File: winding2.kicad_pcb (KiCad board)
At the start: 2 copper layers, 104 x 75.2 mm, 19 parts, among them J1 Screw_Terminal_2_P5.00mm, J2 Limit Switches, J3 Screw Stepper, J4 Main Stepper, J5 RPM & ESC, J6 5V input, J7 ESC XT60, J8 ARDUINO PROG., SW1 RotaryEncoder_Switch, U1 TMC2209_SILENTSTEPSTICK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

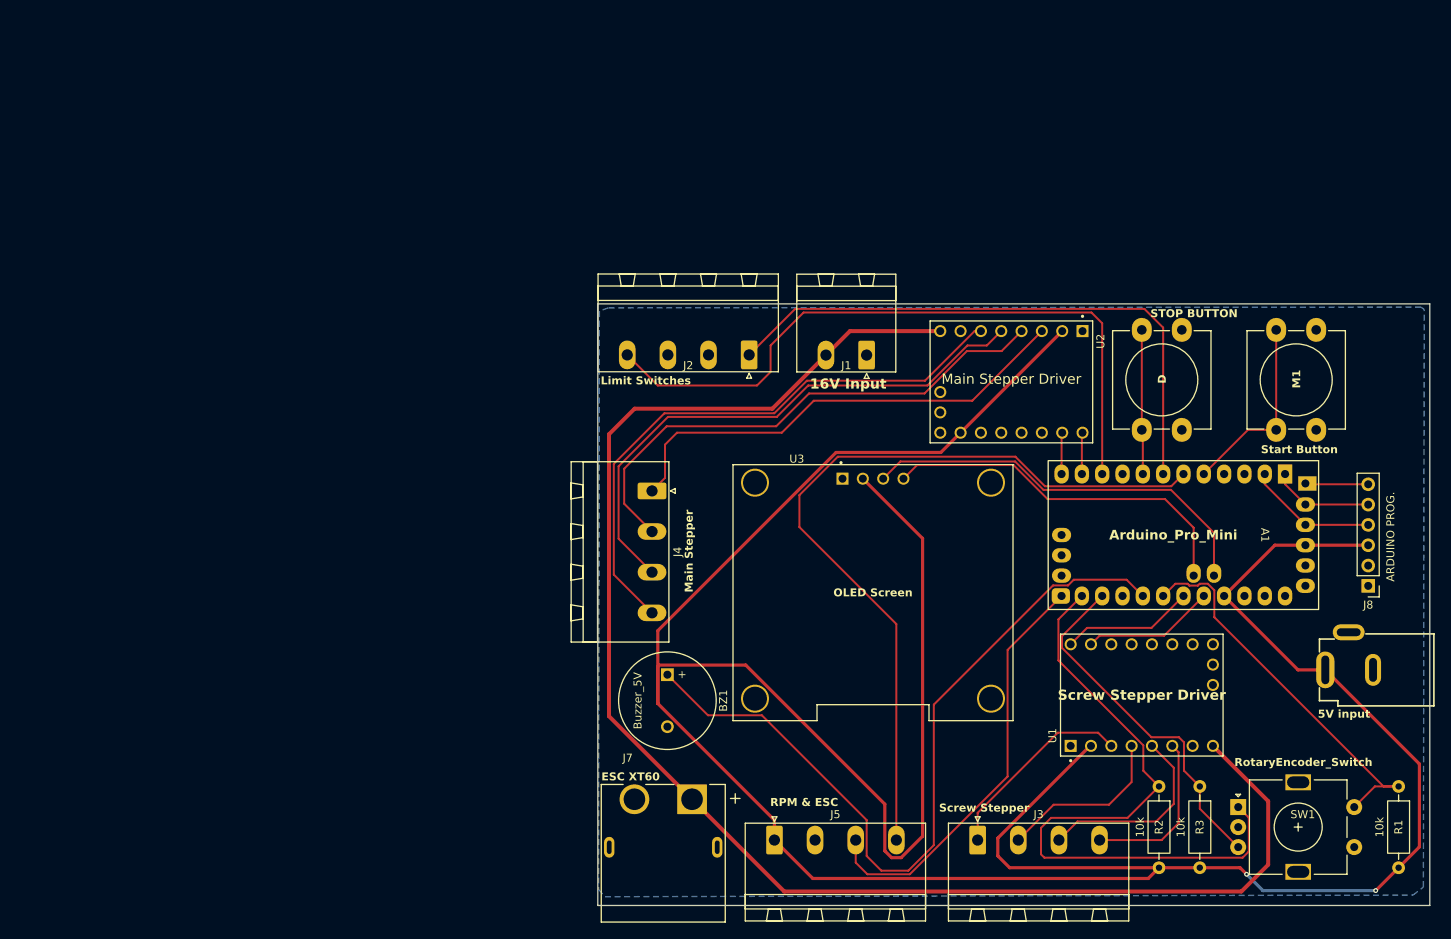
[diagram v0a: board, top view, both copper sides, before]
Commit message: rearranging components to be more user freindly and added front GND Zone
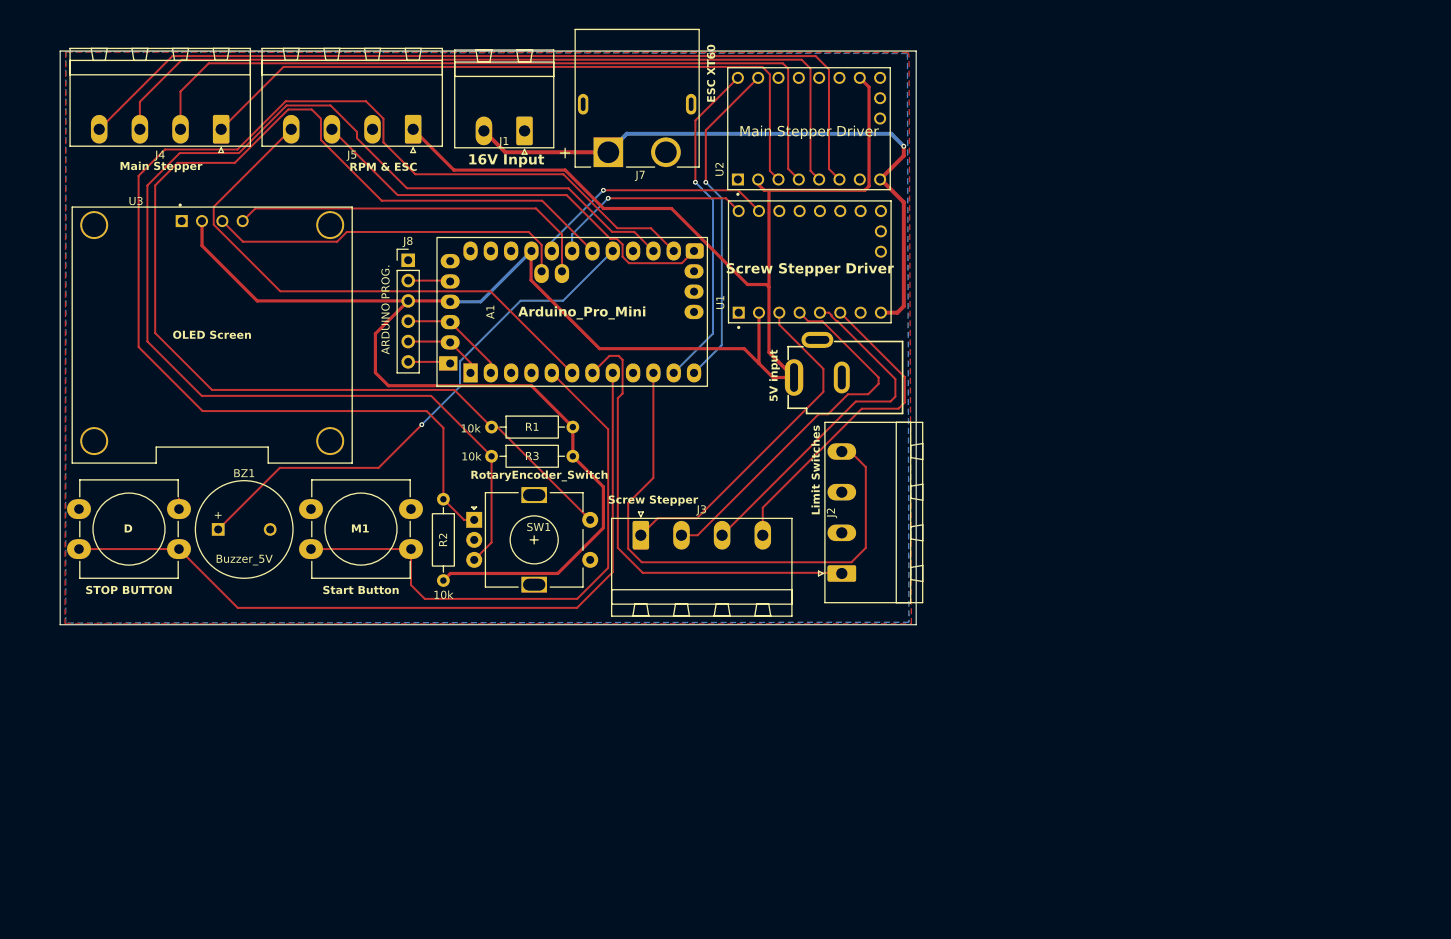
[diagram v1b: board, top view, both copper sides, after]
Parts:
- moved STOP BUTTON 130.4 mm to (56.6, 102.5), turned to 180 degrees
- moved J8 126.7 mm to (91.5, 69.0), turned to 0 degrees
- moved R1 122.0 mm to (101.9, 89.8), turned to 0 degrees
- moved Start Button 118.4 mm to (85.6, 102.5), turned to 180 degrees
- moved A1 102.6 mm to (99.3, 83.0), turned to 90 degrees
- moved SW1 102.0 mm to (99.8, 101.4)
- moved J5 99.7 mm to (92.1, 52.6), turned to 180 degrees
- moved R3 97.7 mm to (101.9, 93.5), turned to 0 degrees
- moved R2 96.4 mm to (95.9, 98.8)
- moved U3 88.7 mm to (67.0, 78.3)
- moved J7 80.9 mm to (120.1, 55.4), turned to 180 degrees
- moved J6 75.8 mm to (145.7, 83.6)
- moved J4 70.3 mm to (68.1, 52.6), turned to 180 degrees
- moved U1 68.2 mm to (141.7, 69.1)
- moved BZ1 59.0 mm to (67.8, 102.6), turned to 0 degrees
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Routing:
- net /ENCODER_B: track 44.6 -> 157.7 mm
- net +16V: track 192.6 -> 81.2 mm, vias 0 -> 1
- net 5V: track 388.5 -> 283.4 mm, vias 2 -> 0
- net /ENCODER_SW: track 49.3 -> 150.0 mm
- net /D_Button: track 18.1 -> 96.5 mm
- net /ENCODER_A: track 83.0 -> 157.8 mm
- net /M1_Button: track 23.8 -> 71.3 mm
- net /DIR1: track 5.20 -> 42.0 mm, vias 0 -> 1
- net /STP1: track 5.20 -> 41.9 mm, vias 0 -> 1
- net /M2B: track 73.4 -> 110.0 mm
- net /M2A: track 69.8 -> 104.2 mm
- net /BUZZ-A0: track 98.4 -> 65.6 mm, vias 0 -> 1
- net /RPM: track 100.3 -> 68.4 mm
- net /M1A: track 66.1 -> 96.8 mm
- net /M1B: track 59.4 -> 85.8 mm
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- added copper zone on F.Cu, net GND
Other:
- board size 104 x 75.2 mm -> 107 x 71.7 mm
- board text added: "version 0.1"
- board text removed: "version 0.0"

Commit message: mounting holes added and errors fixed
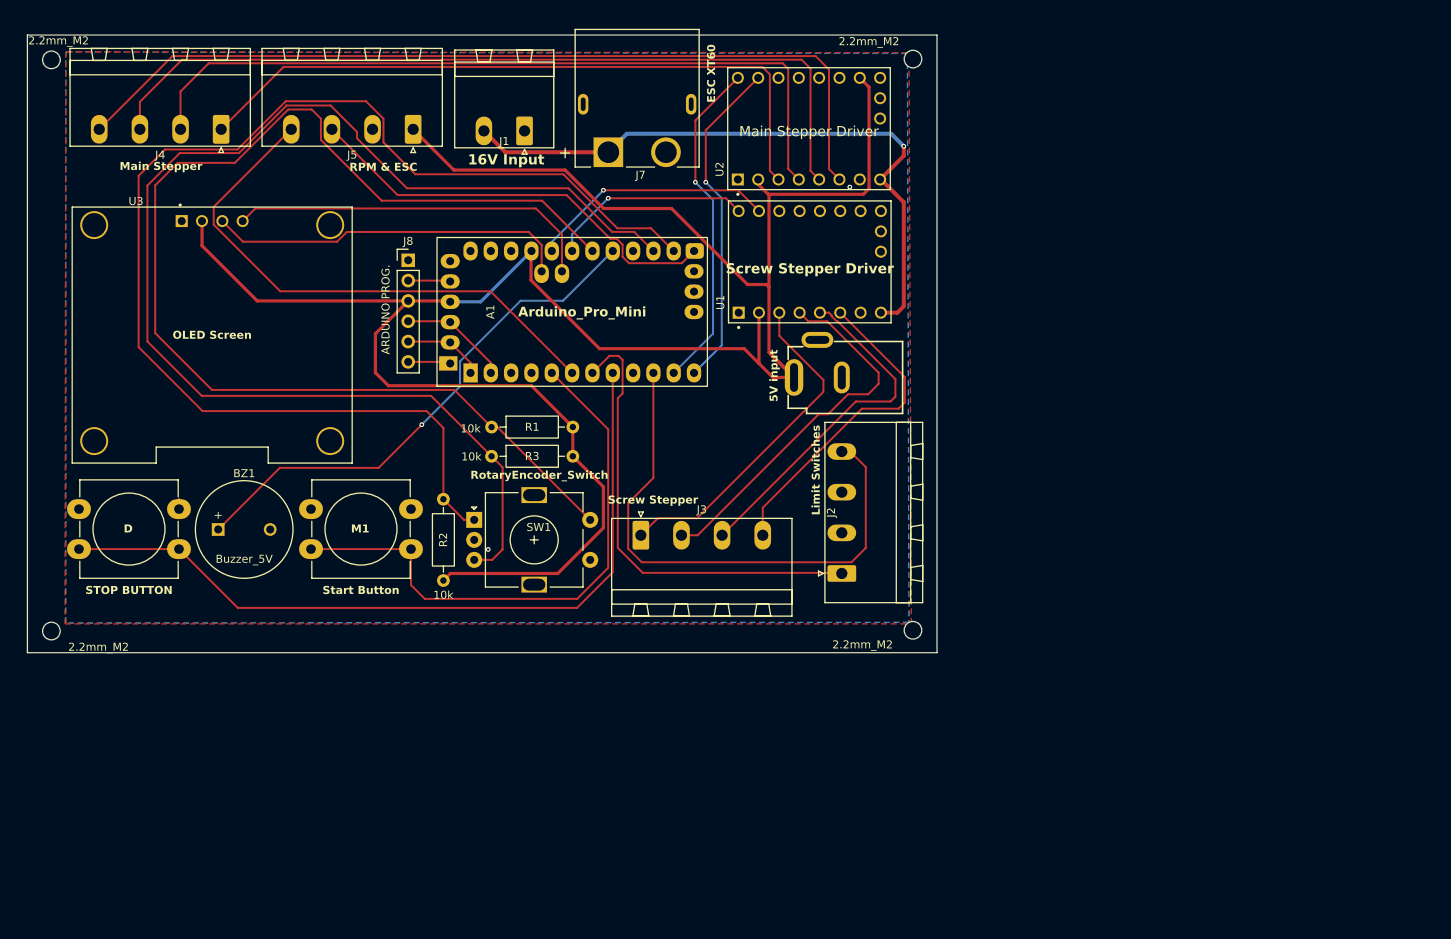
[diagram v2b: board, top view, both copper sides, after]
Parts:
- added 2.2mm_M2: MountingHole_2.2mm_M2, MountingHole:MountingHole_2.2mm_M2, F.Cu at (154.6, 115.2)
- added 2.2mm_M2: MountingHole_2.2mm_M2, MountingHole:MountingHole_2.2mm_M2, F.Cu at (154.6, 43.8)
- added 2.2mm_M2: MountingHole_2.2mm_M2, MountingHole:MountingHole_2.2mm_M2, F.Cu at (46.9, 43.9)
- added 2.2mm_M2: MountingHole_2.2mm_M2, MountingHole:MountingHole_2.2mm_M2, F.Cu at (46.9, 115.3)
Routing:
- net /ENCODER_B: track 157.7 -> 160.2 mm
- net GND: vias 0 -> 2
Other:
- board size 107 x 71.7 mm -> 113.7 x 77.2 mm

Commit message: GND zones modified and board dimensions updated
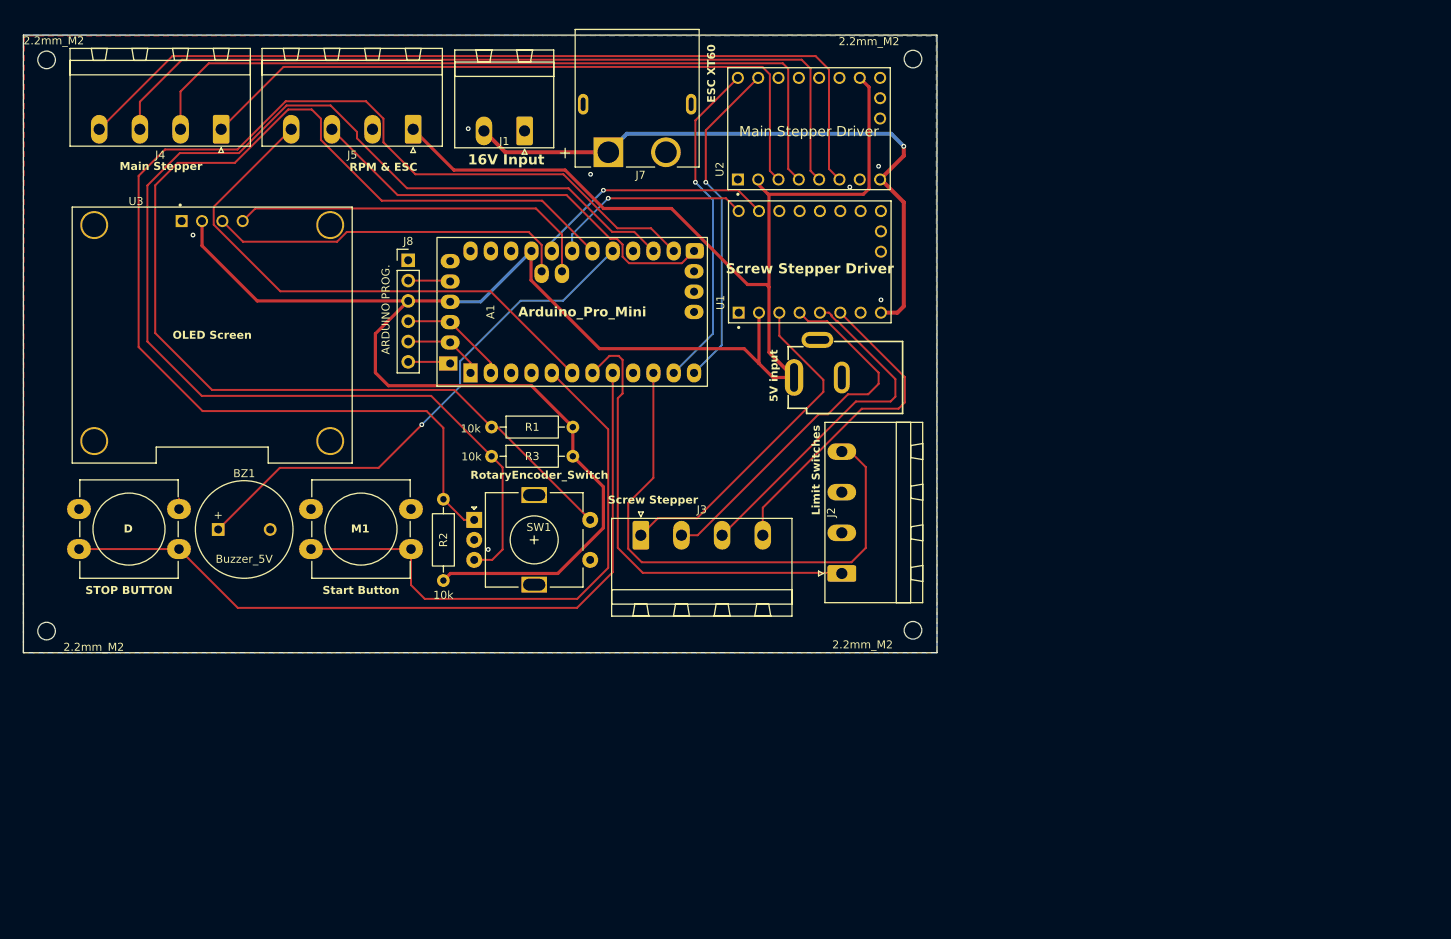
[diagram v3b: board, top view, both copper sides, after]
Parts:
- moved 2.2mm_M2 0.60 mm to (46.3, 43.9)
- moved 2.2mm_M2 0.60 mm to (46.3, 115.3)
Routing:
- net GND: vias 2 -> 7
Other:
- board size 113.7 x 77.2 mm -> 114.2 x 77.2 mm
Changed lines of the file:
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@@
 			(at 0 3.15 0)
 			(layer "F.Fab")
+			(hide yes)
 			(effects
 				(font
@@
 			(layer "F.CrtYd")
 		)
-		(fp_text user "${REFERENCE}"
-			(at 0 0 0)
-			(layer "F.Fab")
-			(effects
-				(font
-					(size 1 1)
-					(thickness 0.15)
-				)
-			)
-		)
 		(pad "" np_thru_hole circle
 			(at 0 0)
@@
 			(at 0 3.15 0)
 			(layer "F.Fab")
+			(hide yes)
 			(effects
 				(font
@@
 			(layer "F.CrtYd")
 		)
-		(fp_text user "${REFERENCE}"
-			(at 0 0 0)
-			(layer "F.Fab")
-			(effects
-				(font
-					(size 1 1)
-					(thickness 0.15)
-				)
-			)
-		)
 		(pad "" np_thru_hole circle
 			(at 0 0)
@@
 	(footprint "MountingHole:MountingHole_2.2mm_M2"
 		(layer "F.Cu")
-		(at 46.902498 43.897502)
+		(at 46.3 43.9)
 		(descr "Mounting Hole 2.2mm, M2, no annular, generated by kicad-footprint-generator mountinghole.py")
 		(tags "mountinghole M2")
@@
 			)
 		)
+		(clearance 0.01)
 		(attr exclude_from_pos_files exclude_from_bom)
 		(fp_circle
@@
 			(fill no)
 			(layer "Cmts.User")
-			(net 65793)
+			(net 121024075)
 		)
 		(fp_circle
@@
 			(fill no)
 			(layer "F.CrtYd")
-			(net 65793)
+			(net 121024075)
 		)
 		(pad "" np_thru_hole circle
@@
 	(footprint "MountingHole:MountingHole_2.2mm_M2"
 		(layer "F.Cu")
-		(at 46.9 115.297502)
+		(at 46.297502 115.3)
 		(descr "Mounting Hole 2.2mm, M2, no annular, generated by kicad-footprint-generator mountinghole.py")
 		(tags "mountinghole M2")
@@
 			(fill no)
 			(layer "Cmts.User")
-			(net 65793)
+			(net 121024075)
 		)
 		(fp_circle
@@
 			(fill no)
 			(layer "F.CrtYd")
-			(net 65793)
+			(net 121024075)
 		)
 		(pad "" np_thru_hole circle
@@
 	)
 	(gr_rect
-		(start 43.9 40.8)
+		(start 43.4 40.8)
 		(end 157.6 118)
 		(stroke
@@
 		(layer "F.Cu")
 		(pts
-			(xy 157.6 118) (xy 43.9 118)
+			(xy 157.6 40.8) (xy 157.6 118)
 		)
-		(height -6.4)
+		(height -11.5)
 		(format
 			(prefix "")
@@
 			(keep_text_aligned yes)
 		)
-		(gr_text "113.7"
-			(at 100.75 122.6 0)
+		(gr_text "77.2"
+			(at 167.3 79.4 90)
 			(layer "F.Cu")
 			(effects
@@
 	)
 	(dimension
-		(type aligned)
+		(type orthogonal)
 		(layer "F.Cu")
 		(pts
-			(xy 157.6 40.8) (xy 157.6 118)
+			(xy 43.4 118) (xy 157.6 118)
 		)
-		(height -11.5)
+		(height 4.8)
+		(orientation 0)
 		(format
 			(prefix "")
@@
 		)
 		(style
-			(thickness 0.2)
+			(thickness 0.05)
 			(arrow_length 1.27)
 			(text_position_mode 0)
@@
 			(keep_text_aligned yes)
 		)
-		(gr_text "77.2"
-			(at 167.3 79.4 90)
+		(gr_text "114.2"
+			(at 100.5 121.65 0)
 			(layer "F.Cu")
 			(effects
 				(font
-					(size 1.5 1.5)
-					(thickness 0.3)
+					(size 1 1)
+					(thickness 0.15)
 				)
 			)
@@
 	)
 	(via
+		(at 64.6 65.8)
+		(size 0.6)
+		(drill 0.3)
+		(layers "F.Cu" "B.Cu")
+		(free yes)
+		(net 16)
+	)
+	(via
+		(at 150.6 73.9)
+		(size 0.6)
+		(drill 0.3)
+		(layers "F.Cu" "B.Cu")
+		(free yes)
+		(net 16)
+	)
+	(via
 		(at 146.7 59.8)
 		(size 0.6)
@@
 		(net 16)
 	)
+	(via
+		(at 114.3 58.2)
+		(size 0.6)
+		(drill 0.3)
+		(layers "F.Cu" "B.Cu")
+		(free yes)
+		(net 16)
+	)
+	(via
+		(at 99 52.5)
+		(size 0.6)
+		(drill 0.3)
+		(layers "F.Cu" "B.Cu")
+		(free yes)
+		(net 16)
+	)
+	(via
+		(at 150.3 57.2)
+		(size 0.6)
+		(drill 0.3)
+		(layers "F.Cu" "B.Cu")
+		(free yes)
+		(net 16)
+	)
 	(segment
 		(start 116.5 90.08)
@@
 		(polygon
 			(pts
-				(xy 154 43) (xy 48.7 42.9) (xy 48.6 114.4) (xy 154.4 114.4) (xy 154.1 43.3)
+				(xy 157.6 40.8) (xy 43.5 40.9) (xy 43.4 118) (xy 157.6 118) (xy 157.6 40.8)
 			)
 		)
@@
 		(polygon
 			(pts
-				(xy 153.9 43.1) (xy 154.1 114.2) (xy 48.7 114.3) (xy 48.7 42.9)
+				(xy 157.5 40.9) (xy 157.6 118) (xy 43.4 118) (xy 43.4 40.8)
 			)
 		)

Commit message: mounting holes dimensions changed to M3 and edge cuts layer changed to curved one
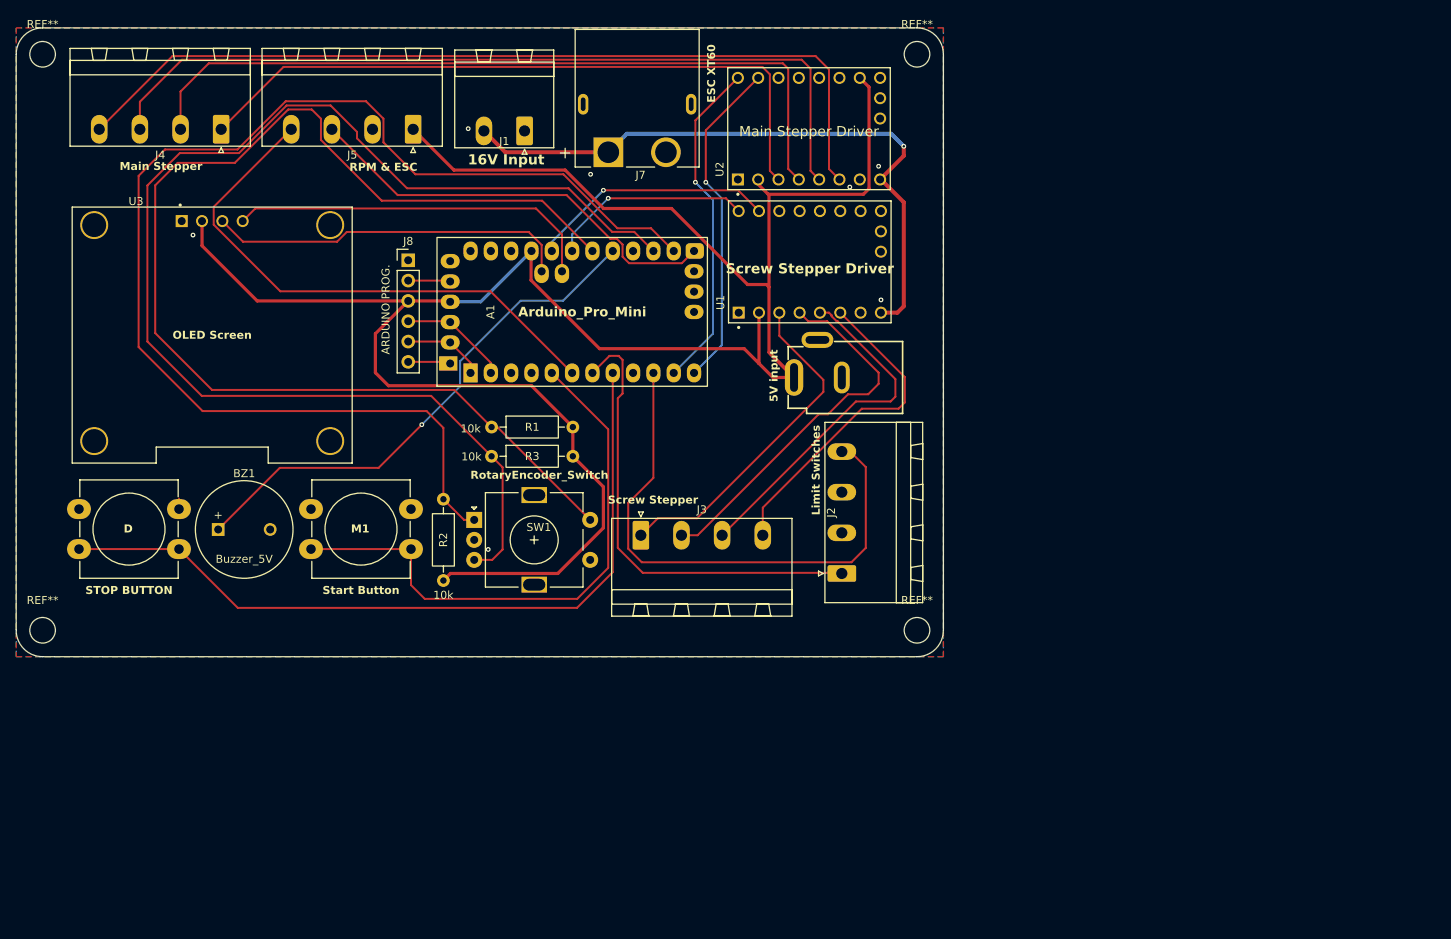
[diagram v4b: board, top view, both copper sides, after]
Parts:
- removed 2.2mm_M2 (x4): MountingHole_2.2mm_M2, MountingHole:MountingHole_2.2mm_M2
- added REF**: MountingHole_3.2mm_M3_DIN965, MountingHole:MountingHole_3.2mm_M3_DIN965, F.Cu at (155.1, 115.2)
- added REF**: MountingHole_3.2mm_M3_DIN965, MountingHole:MountingHole_3.2mm_M3_DIN965, F.Cu at (45.8, 115.2)
- added REF**: MountingHole_3.2mm_M3_DIN965, MountingHole:MountingHole_3.2mm_M3_DIN965, F.Cu at (45.8, 43.2)
- added REF**: MountingHole_3.2mm_M3_DIN965, MountingHole:MountingHole_3.2mm_M3_DIN965, F.Cu at (155.1, 43.2)
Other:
- board size 114.2 x 77.2 mm -> 115.9 x 78.6 mm
